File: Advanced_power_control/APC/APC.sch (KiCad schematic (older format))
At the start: 19 parts

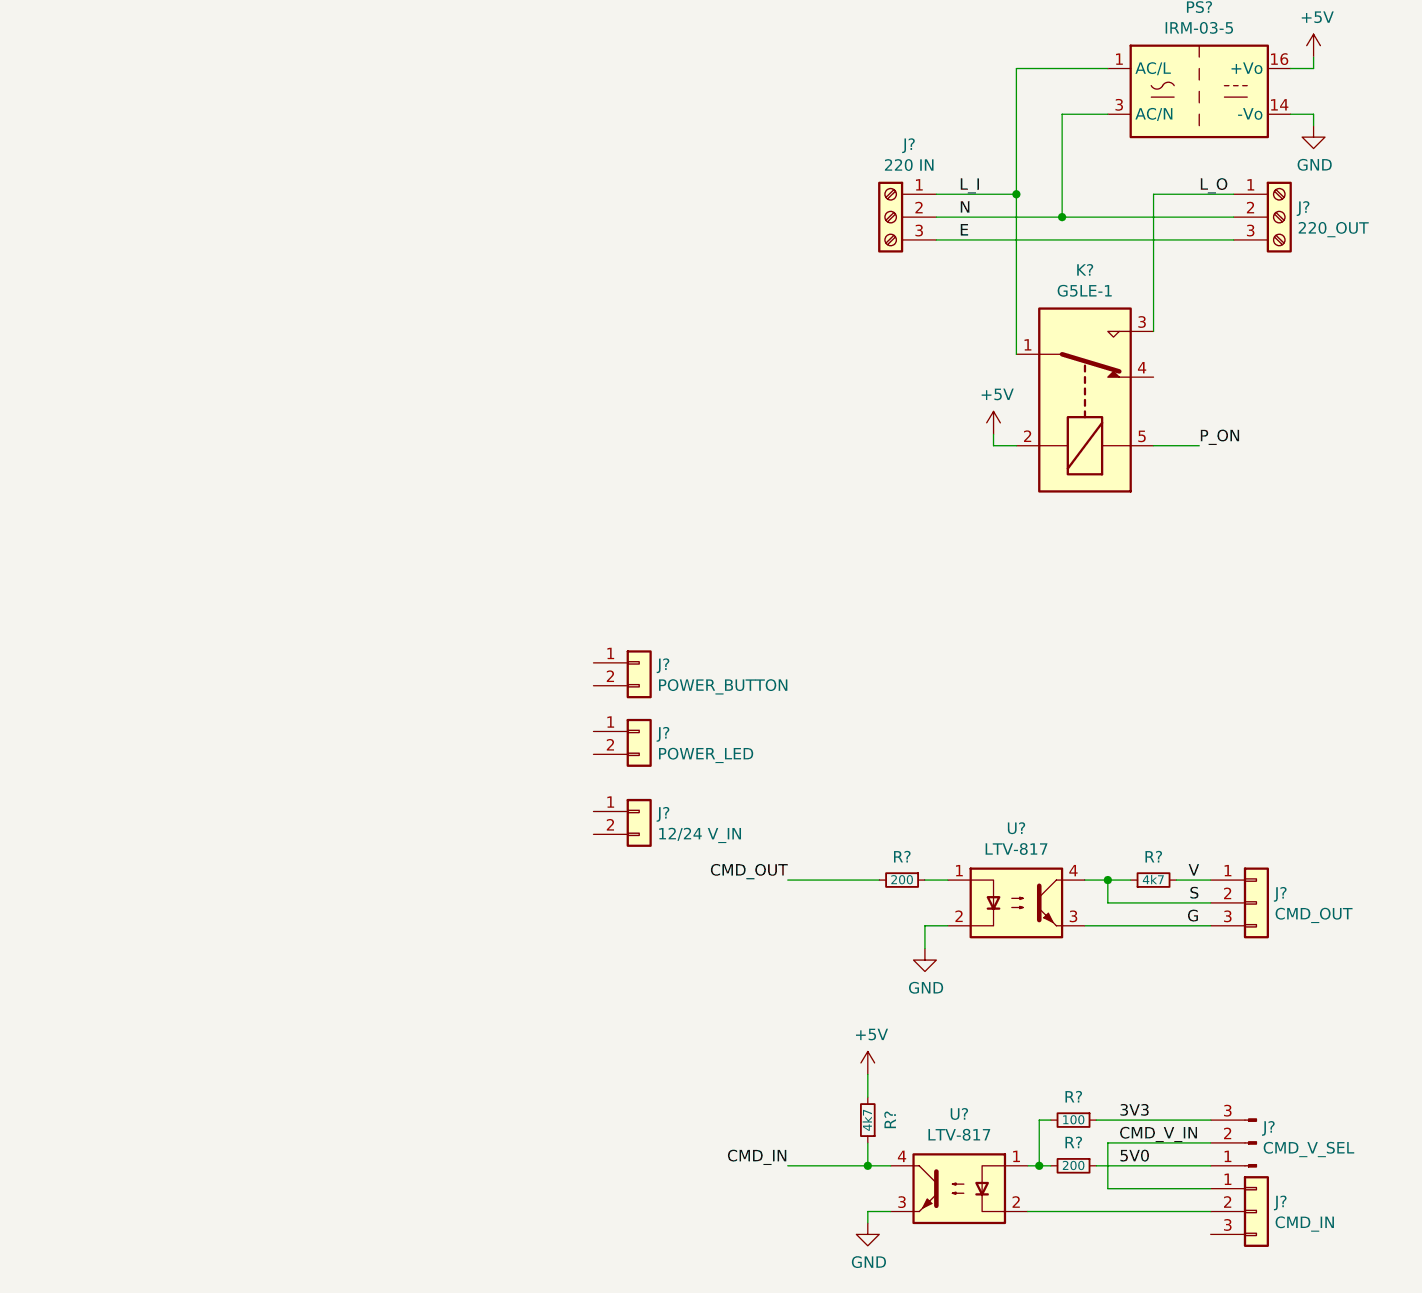
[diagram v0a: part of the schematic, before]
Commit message: update schematic
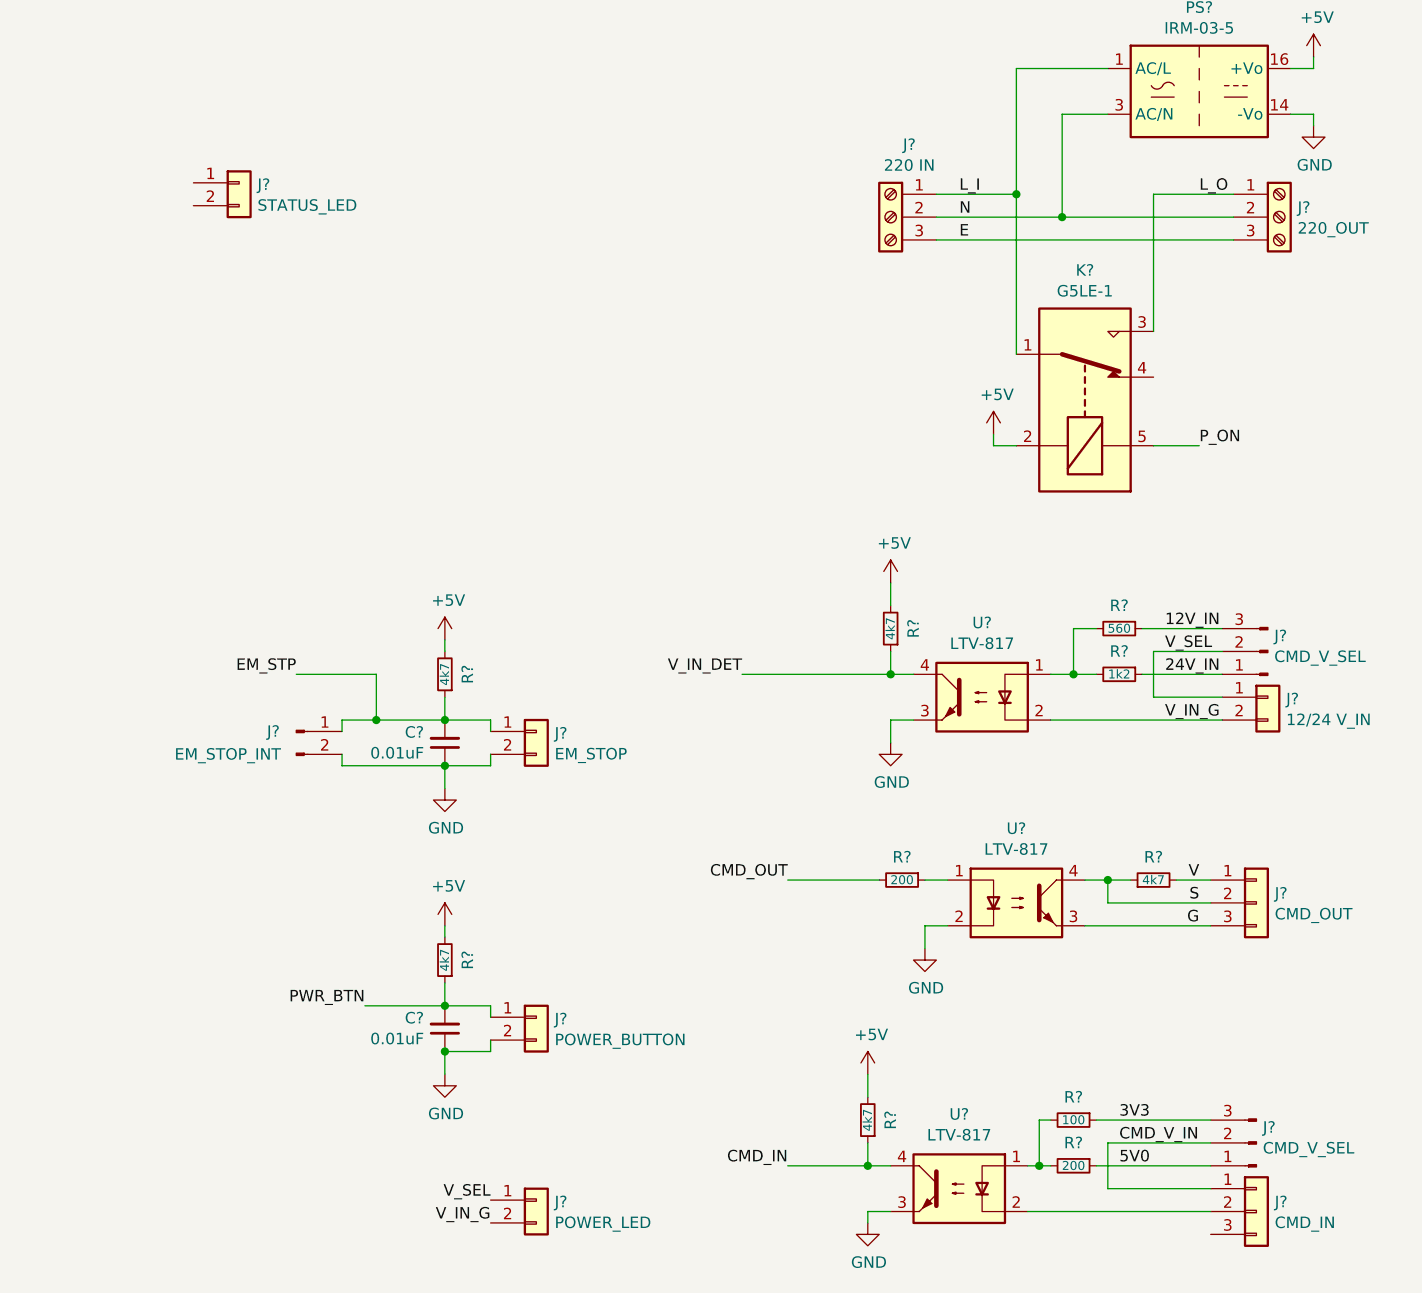
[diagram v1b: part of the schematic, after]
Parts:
- added C? (x2): 0.01uF, symbol Device:C_Small
- added J?: EM_STOP, symbol Connector_Generic:Conn_01x02
- added J?: STATUS_LED, symbol Connector_Generic:Conn_01x02
- added J?: CMD_V_SEL, symbol Connector:Conn_01x03_Male
- added J?: EM_STOP_INT, symbol Connector:Conn_01x02_Male
- added R?: 1k2, symbol Device:R_Small
- added R?: 560, symbol Device:R_Small
- added R? (x3): 4k7, symbol Device:R_Small
- added U?: LTV-817, Package_DIP:DIP-4_W7.62mm, symbol Isolator:LTV-817
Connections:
- net +5V: now also R?.2, R?.2, R?.2
- net GND: now also J?.2 (Pin_2), C?.1, C?.1, J?.2 (Pin_2), J?.2 (Pin_2), U?.3
- net PWR_BTN: now reaches J?.1 (Pin_1)
- net PWR_BTN: now also C?.2, R?.1
- net V_SEL: now reaches J?.1 (Pin_1)
- net V_SEL: now also J?.1 (Pin_1), J?.2 (Pin_2)
- net V_IN_G: now reaches J?.2 (Pin_2)
- net V_IN_G: now also J?.2 (Pin_2), U?.2
- new net: R?.2, R?.2, U?.1
- new net 12V_IN: J?.3 (Pin_3), R?.1
- new net 24V_IN: J?.1 (Pin_1), R?.1
- new net EM_STP: C?.2, J?.1 (Pin_1), J?.1 (Pin_1), R?.1
- new net V_IN_DET: R?.1, U?.4
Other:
- moved on the sheet: J?

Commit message: add some schematic features
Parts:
- removed J?: AVR-ISP-6, symbol Connector:AVR-ISP-6
- removed J?: STATUS_LED, symbol Connector_Generic:Conn_01x02
- added BZ1: Buzzer, symbol Device:Buzzer
- added C1, C2, C3, C4, C5: 0.01uF, symbol Device:C_Small
- added D1: 1N4148, Diode_THT:D_DO-35_SOD27_P7.62mm_Horizontal, symbol Diode:1N4148
- added J1: AVR-JTAG-10, Connector_IDC:IDC-Header_2x05_P2.54mm_Vertical, symbol Connector:AVR-JTAG-10
- added J3: STATUS_LED, Connector_JST:JST_EH_B2B-EH-A_1x02_P2.50mm_Vertical, symbol Connector_Generic:Conn_01x02
- added Q1, Q2, Q3: IRLML0030, Package_TO_SOT_SMD:SOT-23, symbol Transistor_FET:IRLML0030
- added R1, R3, R6, R7: 4k7, symbol Device:R_Small
- added R2, R4, R5: 200, symbol Device:R_Small
- added R8: 390, symbol Device:R_Small
- J10, J8: renamed from J?; footprint (none) -> Connector_JST:JST_EH_B3B-EH-A_1x03_P2.50mm_Vertical
- J11: renamed from J?; value CMD_V_SEL -> PWR_V_SEL; footprint (none) -> Connector_PinHeader_2.54mm:PinHeader_1x03_P2.54mm_Vertical
- J12, J2, J4, J5, J6: renamed from J?; footprint (none) -> Connector_JST:JST_EH_B2B-EH-A_1x02_P2.50mm_Vertical
- J9: renamed from J?; footprint (none) -> Connector_PinHeader_2.54mm:PinHeader_1x03_P2.54mm_Vertical
- gave numbers to parts that had none: 20
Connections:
- net +5V: now also U1.17 (VCC), U1.27 (AVCC), U1.38 (VCC), U1.5 (VCC), BZ1.1 (-), C3.2, C4.2, C5.2, D1.1 (K), J1.4 (VREF), J1.7 (VCC), R1.2, R8.2
- net CMD_IN: now also U1.43 (PB3)
- net CMD_OUT: now also U1.34 (PA3)
- net EM_STP: now also U1.41 (PB1)
- net GND: now also U1.18 (GND), U1.28 (GND), U1.39 (GND), U1.6 (GND), C1.1, C2.1, C3.1, C4.1, C5.1, J1.10 (GND), J1.2 (GND), Q1.2 (S), Q2.2 (S), Q3.2 (S), R3.1, R6.1, R7.1
- net PWR_BTN: now also U1.40 (PB0)
- net P_ON: now also D1.2 (A), Q2.3 (D)
- net V_IN_DET: now also U1.42 (PB2)
- net TCK: now reaches U1.21 (PC2)
- net TCK: now also J1.1 (TCK)
- net TMS: now reaches U1.22 (PC3)
- net TMS: now also J1.5 (TMS)
- net TDO: now reaches U1.23 (PC4)
- net TDO: now also J1.3 (TDO)
- net TDI: now reaches U1.24 (PC5)
- net TDI: now also J1.9 (TDI)
- net at U1.29 (AREF): now also C2.2
- net PWR: now reaches U1.35 (PA2)
- net PWR: now also R4.2
- net S_STATE: now reaches U1.36 (PA1)
- net S_STATE: now also R2.2
- net STATE: now reaches U1.37 (PA0)
- net STATE: now also R5.2
- net RST: now reaches U1.4 (~RESET)
- net RST: now also C1.2, J1.6 (~SRST), R1.1
- new net: Q3.1 (G), R5.1, R7.2
- new net: J3.2 (Pin_2), Q3.3 (D)
- new net: J3.1 (Pin_1), R8.1
- new net: Q2.1 (G), R4.1, R6.2
- new net: BZ1.2 (+), Q1.3 (D)
- new net: Q1.1 (G), R2.1, R3.2
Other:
- moved on the sheet: U1

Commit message: pcb routing
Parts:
- added C8: 10uF 16V, Capacitor_Tantalum_SMD:CP_EIA-3528-21_Kemet-B_Pad1.50x2.35mm_HandSolder, symbol Device:CP_Small
- BZ1: footprint (none) -> Buzzer_Beeper:Buzzer_12x9.5RM7.6
- C1, C2, C4, C6, C7: footprint (none) -> Capacitor_SMD:C_0805_2012Metric_Pad1.18x1.45mm_HandSolder
- C3, C5: value 0.01uF -> 0.1uF; footprint (none) -> Capacitor_SMD:C_0805_2012Metric_Pad1.18x1.45mm_HandSolder
- J13, J7: footprint (none) -> TerminalBlock_RND:TerminalBlock_RND_205-00013_1x03_P5.00mm_Horizontal
- J2: footprint Connector_JST:JST_EH_B2B-EH-A_1x02_P2.50mm_Vertical -> Connector_PinHeader_2.54mm:PinHeader_1x02_P2.54mm_Vertical
- R1, R10, R11, R12, R13, R14, R15, R16, R17, R18, R2, R3, R4, R5, R6, R7, R8, R9: footprint (none) -> Resistor_SMD:R_0805_2012Metric_Pad1.20x1.40mm_HandSolder
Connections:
- net +5V: now also C8.1
- net EM_STP: now also U1.15 (PD6); no longer U1.41 (PB1)
- net GND: now also C8.2
- net PWR_BTN: now also U1.16 (PD7); no longer U1.40 (PB0)
- net V_IN_DET: now also U1.14 (PD5); no longer U1.42 (PB2)
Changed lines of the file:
@@
 F 0 "J13" H 10730 1692 50  0000 L CNN
 F 1 "220_OUT" H 10730 1601 50  0000 L CNN
-F 2 "" H 10650 1650 50  0001 C CNN
+F 2 "TerminalBlock_RND:TerminalBlock_RND_205-00013_1x03_P5.00mm_Horizontal" H 10650 1650 50  0001 C CNN
 F 3 "~" H 10650 1650 50  0001 C CNN
 	1    10650 1650
@@
 F 0 "J7" H 8868 1967 50  0000 C CNN
 F 1 "220 IN" H 8868 1876 50  0000 C CNN
-F 2 "" H 8950 1650 50  0001 C CNN
+F 2 "TerminalBlock_RND:TerminalBlock_RND_205-00013_1x03_P5.00mm_Horizontal" H 8950 1650 50  0001 C CNN
 F 3 "~" H 8950 1650 50  0001 C CNN
 	1    8950 1650
@@
 F 0 "R15" V 9650 5800 50  0000 C CNN
 F 1 "200" V 9750 5800 39  0000 C CNN
-F 2 "" H 9750 5800 50  0001 C CNN
+F 2 "Resistor_SMD:R_0805_2012Metric_Pad1.20x1.40mm_HandSolder" H 9750 5800 50  0001 C CNN
 F 3 "~" H 9750 5800 50  0001 C CNN
 	1    9750 5800
@@
 F 0 "R14" V 9650 5600 50  0000 C CNN
 F 1 "100" V 9750 5600 39  0000 C CNN
-F 2 "" H 9750 5600 50  0001 C CNN
+F 2 "Resistor_SMD:R_0805_2012Metric_Pad1.20x1.40mm_HandSolder" H 9750 5600 50  0001 C CNN
 F 3 "~" H 9750 5600 50  0001 C CNN
 	1    9750 5600
@@
 F 0 "R11" V 8750 5600 50  0000 C CNN
 F 1 "4k7" V 8850 5600 39  0000 C CNN
-F 2 "" H 8850 5600 50  0001 C CNN
+F 2 "Resistor_SMD:R_0805_2012Metric_Pad1.20x1.40mm_HandSolder" H 8850 5600 50  0001 C CNN
 F 3 "~" H 8850 5600 50  0001 C CNN
 	1    8850 5600
@@
 F 0 "R18" V 10200 4550 50  0000 C CNN
 F 1 "4k7" V 10100 4550 39  0000 C CNN
-F 2 "" H 10100 4550 50  0001 C CNN
+F 2 "Resistor_SMD:R_0805_2012Metric_Pad1.20x1.40mm_HandSolder" H 10100 4550 50  0001 C CNN
 F 3 "~" H 10100 4550 50  0001 C CNN
 	1    10100 4550
@@
 F 0 "R13" V 8900 4550 50  0000 C CNN
 F 1 "200" V 9000 4550 39  0000 C CNN
-F 2 "" H 9000 4550 50  0001 C CNN
+F 2 "Resistor_SMD:R_0805_2012Metric_Pad1.20x1.40mm_HandSolder" H 9000 4550 50  0001 C CNN
 F 3 "~" H 9000 4550 50  0001 C CNN
 	1    9000 4550
@@
 F 0 "R17" V 9850 3650 50  0000 C CNN
 F 1 "1k2" V 9950 3650 39  0000 C CNN
-F 2 "" H 9950 3650 50  0001 C CNN
+F 2 "Resistor_SMD:R_0805_2012Metric_Pad1.20x1.40mm_HandSolder" H 9950 3650 50  0001 C CNN
 F 3 "~" H 9950 3650 50  0001 C CNN
 	1    9950 3650
@@
 F 0 "R16" V 9850 3450 50  0000 C CNN
 F 1 "560" V 9950 3450 39  0000 C CNN
-F 2 "" H 9950 3450 50  0001 C CNN
+F 2 "Resistor_SMD:R_0805_2012Metric_Pad1.20x1.40mm_HandSolder" H 9950 3450 50  0001 C CNN
 F 3 "~" H 9950 3450 50  0001 C CNN
 	1    9950 3450
@@
 F 0 "R12" V 8850 3450 50  0000 C CNN
 F 1 "4k7" V 8950 3450 39  0000 C CNN
-F 2 "" H 8950 3450 50  0001 C CNN
+F 2 "Resistor_SMD:R_0805_2012Metric_Pad1.20x1.40mm_HandSolder" H 8950 3450 50  0001 C CNN
 F 3 "~" H 8950 3450 50  0001 C CNN
 	1    8950 3450
@@
 F 0 "R10" V 6900 4900 50  0000 C CNN
 F 1 "4k7" V 7000 4900 39  0000 C CNN
-F 2 "" H 7000 4900 50  0001 C CNN
+F 2 "Resistor_SMD:R_0805_2012Metric_Pad1.20x1.40mm_HandSolder" H 7000 4900 50  0001 C CNN
 F 3 "~" H 7000 4900 50  0001 C CNN
 	1    7000 4900
@@
 F 0 "C7" H 6909 5154 50  0000 R CNN
 F 1 "0.01uF" H 6909 5245 50  0000 R CNN
-F 2 "" H 7000 5200 50  0001 C CNN
+F 2 "Capacitor_SMD:C_0805_2012Metric_Pad1.18x1.45mm_HandSolder" H 7000 5200 50  0001 C CNN
 F 3 "~" H 7000 5200 50  0001 C CNN
 	1    7000 5200
@@
 F 0 "R9" V 6900 3650 50  0000 C CNN
 F 1 "4k7" V 7000 3650 39  0000 C CNN
-F 2 "" H 7000 3650 50  0001 C CNN
+F 2 "Resistor_SMD:R_0805_2012Metric_Pad1.20x1.40mm_HandSolder" H 7000 3650 50  0001 C CNN
 F 3 "~" H 7000 3650 50  0001 C CNN
 	1    7000 3650
@@
 F 0 "C6" H 6909 3904 50  0000 R CNN
 F 1 "0.01uF" H 6909 3995 50  0000 R CNN
-F 2 "" H 7000 3950 50  0001 C CNN
+F 2 "Capacitor_SMD:C_0805_2012Metric_Pad1.18x1.45mm_HandSolder" H 7000 3950 50  0001 C CNN
 F 3 "~" H 7000 3950 50  0001 C CNN
 	1    7000 3950
@@
 F 0 "J2" H 6250 3900 50  0000 C CNN
 F 1 "EM_STOP_INT" H 6050 3800 50  0000 C CNN
-F 2 "Connector_JST:JST_EH_B2B-EH-A_1x02_P2.50mm_Vertical" H 6350 3900 50  0001 C CNN
+F 2 "Connector_PinHeader_2.54mm:PinHeader_1x02_P2.54mm_Vertical" H 6350 3900 50  0001 C CNN
 F 3 "~" H 6350 3900 50  0001 C CNN
 	1    6350 3900
@@
 F 0 "R5" V 6300 2550 50  0000 C CNN
 F 1 "200" V 6400 2550 39  0000 C CNN
-F 2 "" H 6400 2550 50  0001 C CNN
+F 2 "Resistor_SMD:R_0805_2012Metric_Pad1.20x1.40mm_HandSolder" H 6400 2550 50  0001 C CNN
 F 3 "~" H 6400 2550 50  0001 C CNN
 	1    6400 2550
@@
 F 0 "R7" V 6500 2700 50  0000 C CNN
 F 1 "4k7" V 6600 2700 39  0000 C CNN
-F 2 "" H 6600 2700 50  0001 C CNN
+F 2 "Resistor_SMD:R_0805_2012Metric_Pad1.20x1.40mm_HandSolder" H 6600 2700 50  0001 C CNN
 F 3 "~" H 6600 2700 50  0001 C CNN
 	1    6600 2700
@@
 F 0 "R8" V 6900 2050 50  0000 C CNN
 F 1 "390" V 7000 2050 39  0000 C CNN
-F 2 "" H 7000 2050 50  0001 C CNN
+F 2 "Resistor_SMD:R_0805_2012Metric_Pad1.20x1.40mm_HandSolder" H 7000 2050 50  0001 C CNN
 F 3 "~" H 7000 2050 50  0001 C CNN
 	1    7000 2050
@@
 F 0 "R4" V 6300 950 50  0000 C CNN
 F 1 "200" V 6400 950 39  0000 C CNN
-F 2 "" H 6400 950 50  0001 C CNN
+F 2 "Resistor_SMD:R_0805_2012Metric_Pad1.20x1.40mm_HandSolder" H 6400 950 50  0001 C CNN
 F 3 "~" H 6400 950 50  0001 C CNN
 	1    6400 950
@@
 F 0 "R6" V 6500 1100 50  0000 C CNN
 F 1 "4k7" V 6600 1100 39  0000 C CNN
-F 2 "" H 6600 1100 50  0001 C CNN
+F 2 "Resistor_SMD:R_0805_2012Metric_Pad1.20x1.40mm_HandSolder" H 6600 1100 50  0001 C CNN
 F 3 "~" H 6600 1100 50  0001 C CNN
 	1    6600 1100
@@
 F 0 "BZ1" H 5702 1029 50  0000 L CNN
 F 1 "Buzzer" H 5702 938 50  0000 L CNN
-F 2 "" V 5525 1100 50  0001 C CNN
+F 2 "Buzzer_Beeper:Buzzer_12x9.5RM7.6" V 5525 1100 50  0001 C CNN
 F 3 "~" V 5525 1100 50  0001 C CNN
 	1    5550 1000
@@
 F 0 "R2" V 4550 1300 50  0000 C CNN
 F 1 "200" V 4650 1300 39  0000 C CNN
-F 2 "" H 4650 1300 50  0001 C CNN
+F 2 "Resistor_SMD:R_0805_2012Metric_Pad1.20x1.40mm_HandSolder" H 4650 1300 50  0001 C CNN
 F 3 "~" H 4650 1300 50  0001 C CNN
 	1    4650 1300
@@
 F 0 "R3" V 4750 1450 50  0000 C CNN
 F 1 "4k7" V 4850 1450 39  0000 C CNN
-F 2 "" H 4850 1450 50  0001 C CNN
+F 2 "Resistor_SMD:R_0805_2012Metric_Pad1.20x1.40mm_HandSolder" H 4850 1450 50  0001 C CNN
 F 3 "~" H 4850 1450 50  0001 C CNN
 	1    4850 1450
@@
 F 0 "C4" H 2659 2854 50  0000 R CNN
 F 1 "0.01uF" H 2659 2945 50  0000 R CNN
-F 2 "" H 2750 2900 50  0001 C CNN
+F 2 "Capacitor_SMD:C_0805_2012Metric_Pad1.18x1.45mm_HandSolder" H 2750 2900 50  0001 C CNN
 F 3 "~" H 2750 2900 50  0001 C CNN
 	1    2750 2900
@@
 P 3250 2900
 F 0 "C5" H 3159 2854 50  0000 R CNN
-F 1 "0.01uF" H 3159 2945 50  0000 R CNN
-F 2 "" H 3250 2900 50  0001 C CNN
+F 1 "0.1uF" H 3159 2945 50  0000 R CNN
+F 2 "Capacitor_SMD:C_0805_2012Metric_Pad1.18x1.45mm_HandSolder" H 3250 2900 50  0001 C CNN
 F 3 "~" H 3250 2900 50  0001 C CNN
 	1    3250 2900
@@
 P 2450 2900
 F 0 "C3" H 2359 2854 50  0000 R CNN
-F 1 "0.01uF" H 2359 2945 50  0000 R CNN
-F 2 "" H 2450 2900 50  0001 C CNN
+F 1 "0.1uF" H 2359 2945 50  0000 R CNN
+F 2 "Capacitor_SMD:C_0805_2012Metric_Pad1.18x1.45mm_HandSolder" H 2450 2900 50  0001 C CNN
 F 3 "~" H 2450 2900 50  0001 C CNN
 	1    2450 2900
@@
 F 0 "R1" V 1750 3300 50  0000 C CNN
 F 1 "4k7" V 1850 3300 39  0000 C CNN
-F 2 "" H 1850 3300 50  0001 C CNN
+F 2 "Resistor_SMD:R_0805_2012Metric_Pad1.20x1.40mm_HandSolder" H 1850 3300 50  0001 C CNN
 F 3 "~" H 1850 3300 50  0001 C CNN
 	1    1850 3300
@@
 F 0 "C1" H 1759 3554 50  0000 R CNN
 F 1 "0.01uF" H 1759 3645 50  0000 R CNN
-F 2 "" H 1850 3600 50  0001 C CNN
+F 2 "Capacitor_SMD:C_0805_2012Metric_Pad1.18x1.45mm_HandSolder" H 1850 3600 50  0001 C CNN
 F 3 "~" H 1850 3600 50  0001 C CNN
 	1    1850 3600
@@
 F 0 "C2" H 1759 4154 50  0000 R CNN
 F 1 "0.01uF" H 1759 4245 50  0000 R CNN
-F 2 "" H 1850 4200 50  0001 C CNN
+F 2 "Capacitor_SMD:C_0805_2012Metric_Pad1.18x1.45mm_HandSolder" H 1850 4200 50  0001 C CNN
 F 3 "~" H 1850 4200 50  0001 C CNN
 	1    1850 4200
@@
 Text Label 3450 3750 0    50   ~ 0
 CMD_OUT
-Text Label 3450 4350 0    50   ~ 0
+Text Label 3450 6850 0    50   ~ 0
 PWR_BTN
-Text Label 3450 4450 0    50   ~ 0
+Text Label 3450 6750 0    50   ~ 0
 EM_STP
-Text Label 3450 4550 0    50   ~ 0
+Text Label 3450 6650 0    50   ~ 0
 V_IN_DET
 Text Label 3450 4650 0    50   ~ 0
 CMD_IN
+$Comp
+L Device:CP_Small C8
+U 1 1 608AF908
+P 10950 1100
+F 0 "C8" H 10862 1146 50  0000 R CNN
+F 1 "10uF 16V" H 10862 1055 50  0000 R CNN
+F 2 "Capacitor_Tantalum_SMD:CP_EIA-3528-21_Kemet-B_Pad1.50x2.35mm_HandSolder" H 10950 1100 50  0001 C CNN
+F 3 "~" H 10950 1100 50  0001 C CNN
+	1    10950 1100
+	-1   0    0    -1
+$EndComp
+Wire Wire Line
+	10950 1000 10800 1000
+Connection ~ 10800 1000
+Wire Wire Line
+	10950 1200 10800 1200
+Connection ~ 10800 1200
 $EndSCHEMATC
